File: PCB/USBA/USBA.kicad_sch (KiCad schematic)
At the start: 23 parts, among them J1 USB_A, J2 Shelly, U2 ESP32-S3-MINI-1, U5 MD8942, U7 SHT40

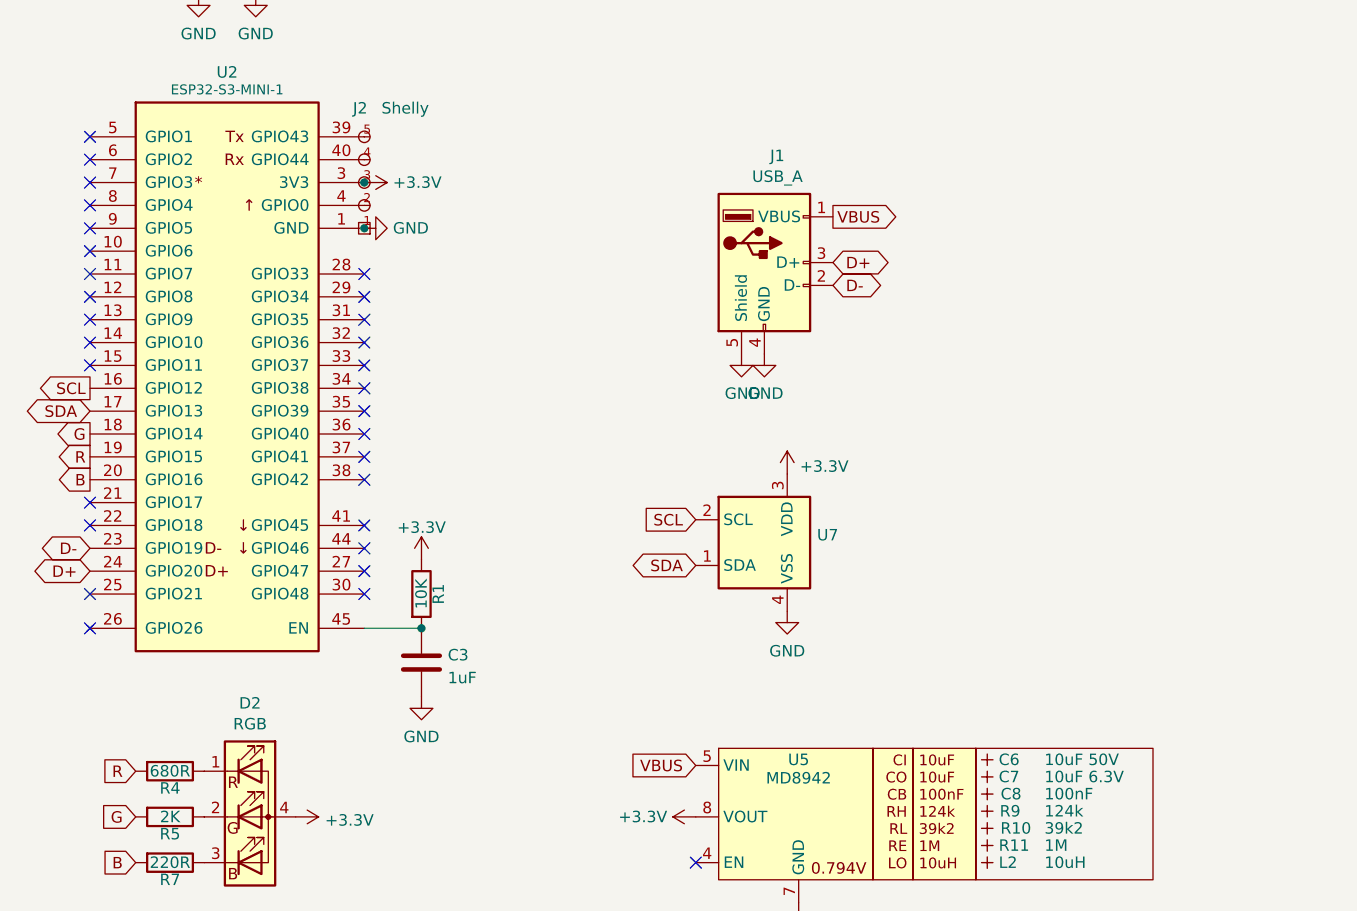
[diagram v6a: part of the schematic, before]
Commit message: Added USB pads to allow programming in panel
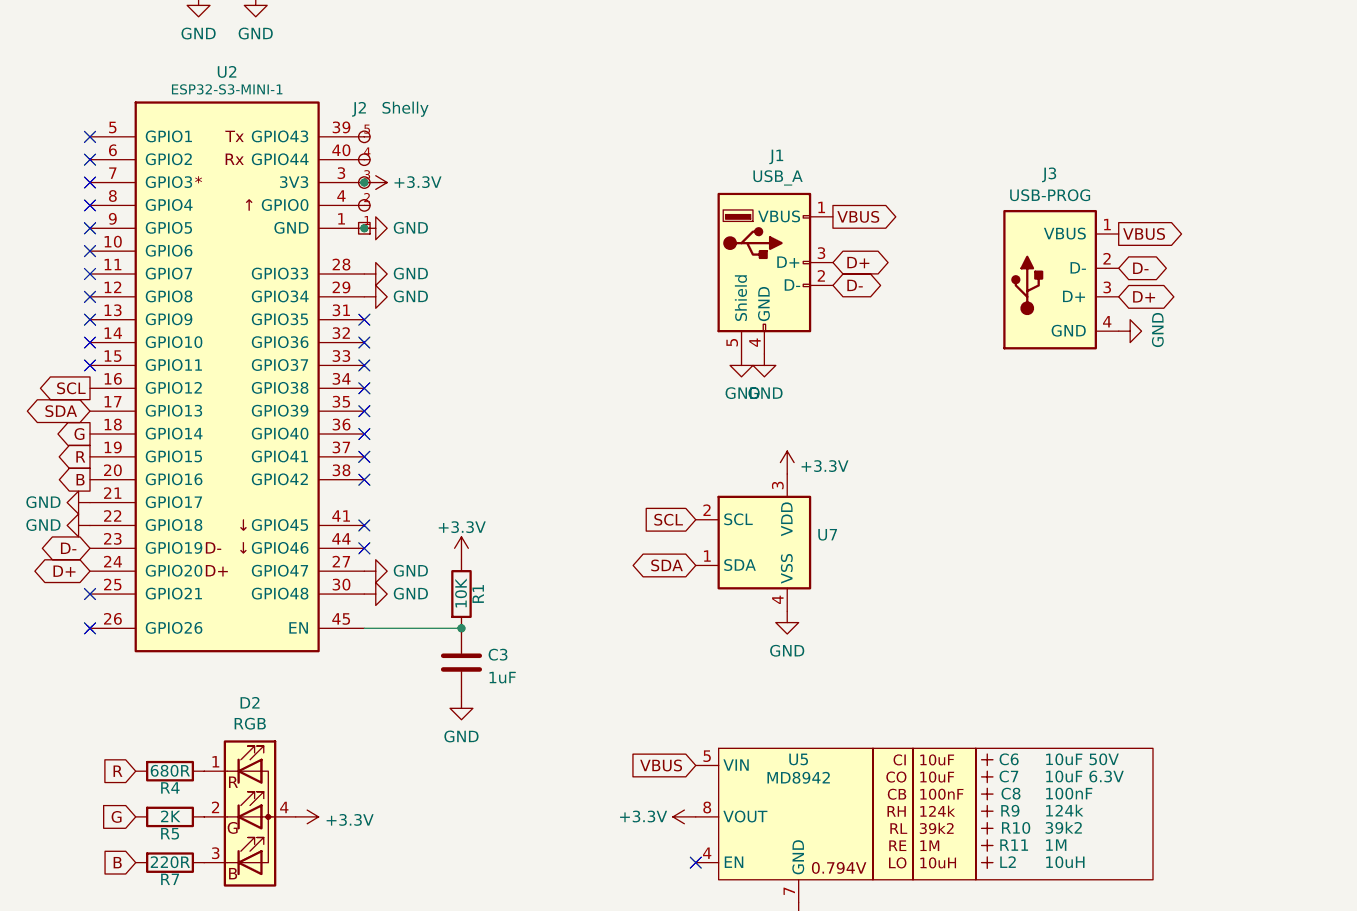
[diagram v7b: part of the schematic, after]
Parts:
- added J3: USB-PROG, RevK:USB-PROG, symbol RevK:USB-PROG
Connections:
- net D+: now also J3.3 (D+)
- net D-: now also J3.2 (D-)
- net GND: now also U2.21 (GPIO17), U2.22 (GPIO18), U2.27 (GPIO47), U2.28 (GPIO33), U2.29 (GPIO34), U2.30 (GPIO48), J3.4 (GND)
- net VBUS: now also J3.1 (VBUS)
- no-connect marks 30 -> 24
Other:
- moved on the sheet: C3, R1

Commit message: Tidy
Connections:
- net GND: now also U2.44 (GPIO46)
- no-connect marks 24 -> 23
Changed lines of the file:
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@@
   (no_connect (at 124.46 75.565))
   (no_connect (at 93.98 57.785))
-  (no_connect (at 124.46 98.425))
   (no_connect (at 161.29 133.35))
   (no_connect (at 124.46 83.185))
@@
         )
       )
+    )
+  )
+  (symbol (lib_id "power:GND") (at 124.46 98.425 90) (unit 1)
+    (in_bom yes) (on_board yes) (dnp no) (fields_autoplaced)
+    (property "Reference" "#PWR021" (at 130.81 98.425 0)
+      (effects (font (size 1.27 1.27)) hide)
+    )
+    (property "Value" "GND" (at 127.635 98.425 90)
+      (effects (font (size 1.27 1.27)) (justify right))
+    )
+    (property "Footprint" "" (at 124.46 98.425 0)
+      (effects (font (size 1.27 1.27)) hide)
+    )
+    (property "Datasheet" "" (at 124.46 98.425 0)
+      (effects (font (size 1.27 1.27)) hide)
+    )
+    (pin "1")
+    (instances
+      (project "USBA"
+        (path "/2d210a96-f81f-42a9-8bf4-1b43c11086f3"
+          (reference "#PWR021") (unit 1)
+        )
+      )
